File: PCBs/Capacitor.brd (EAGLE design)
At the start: 10 x 29.3 mm, 3 parts

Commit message: Updated
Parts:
- moved U$1 0.79 mm to (8.77, 19.9)
- moved C1 0.77 mm to (8.76, 12.1)
- moved U$2 0.76 mm to (8.76, 4.57)
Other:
- board size 10 x 29.3 mm -> 14.5 x 36.5 mm
- board text added: "care@pinwheel.in"
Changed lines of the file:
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@@
 <setting verticaltext="up"/>
 </settings>
-<grid distance="50" unitdist="mil" unit="mm" style="lines" multiple="1" display="yes" altdistance="5" altunitdist="mil" altunit="mm"/>
+<grid distance="0.5" unitdist="mm" unit="mm" style="lines" multiple="1" display="yes" altdistance="5" altunitdist="mil" altunit="mm"/>
 <layers>
 <layer number="1" name="Top" color="4" fill="1" visible="yes" active="yes"/>
@@
 <layer number="43" name="vRestrict" color="2" fill="10" visible="yes" active="yes"/>
 <layer number="44" name="Drills" color="7" fill="1" visible="no" active="yes"/>
-<layer number="45" name="Holes" color="7" fill="1" visible="no" active="yes"/>
+<layer number="45" name="Holes" color="7" fill="1" visible="yes" active="yes"/>
 <layer number="46" name="Milling" color="3" fill="1" visible="no" active="yes"/>
 <layer number="47" name="Measures" color="7" fill="1" visible="no" active="yes"/>
@@
 <board>
 <plain>
-<wire x1="3.048" y1="-2.54" x2="13.081" y2="-2.54" width="0" layer="20"/>
-<wire x1="13.081" y1="-2.54" x2="13.081" y2="26.73" width="0" layer="20"/>
-<wire x1="13.081" y1="26.73" x2="3.048" y2="26.73" width="0" layer="20"/>
-<wire x1="3.048" y1="26.73" x2="3.048" y2="-2.54" width="0" layer="20"/>
+<wire x1="14.292896875" y1="27" x2="3.207103125" y2="27" width="0" layer="20"/>
+<wire x1="3.207103125" y1="27" x2="1.5" y2="25.292896875" width="0" layer="20" curve="90"/>
+<wire x1="1.5" y1="25.292896875" x2="1.5" y2="-0.765165625" width="0" layer="20"/>
+<wire x1="1.5" y1="-0.765165625" x2="3.274834375" y2="-2.54" width="0" layer="20" curve="90"/>
+<wire x1="3.274834375" y1="-2.54" x2="14.225165625" y2="-2.54" width="0" layer="20"/>
+<wire x1="14.225165625" y1="-2.54" x2="16" y2="-0.765165625" width="0" layer="20" curve="90"/>
+<wire x1="16" y1="-0.765165625" x2="16" y2="25.292896875" width="0" layer="20"/>
+<wire x1="16" y1="25.292896875" x2="14.292896875" y2="27" width="0" layer="20" curve="90"/>
 <text x="12.192" y="9.144" size="0.8128" layer="21" rot="R90">Pinwheel Robotics </text>
 <text x="5.461" y="10.541" size="0.8128" layer="21" rot="R90">Capacitor</text>
+<hole x="3.43" y="24.981" drill="3"/>
+<hole x="14.003" y="24.903" drill="3"/>
+<hole x="3.548" y="-0.524" drill="3"/>
+<hole x="14.013" y="-0.54" drill="3"/>
+<wire x1="12" y1="-9" x2="11.5" y2="-9.5" width="0.1524" layer="20"/>
+<text x="15" y="21" size="1.778" layer="22" rot="MR270">care@pinwheel.in</text>
 </plain>
 <attributes>
@@
 </class>
 </classes>
-<designrules name="default">
+<designrules name="default *">
 <description language="de">&lt;b&gt;EAGLE Design Rules&lt;/b&gt;
 &lt;p&gt;
@@
 <param name="mdDrill" value="6mil"/>
 <param name="mdSmdStop" value="0mil"/>
-<param name="msWidth" value="6mil"/>
+<param name="msWidth" value="20mil"/>
 <param name="msDrill" value="0.35mm"/>
 <param name="msMicroVia" value="9.99mm"/>
@@
 <autorouter>
 <pass name="Default">
-<param name="RoutingGrid" value="50mil"/>
+<param name="RoutingGrid" value="0.25mm"/>
 <param name="AutoGrid" value="1"/>
 <param name="Efforts" value="0"/>
@@
 <param name="PrefDir.14" value="0"/>
 <param name="PrefDir.15" value="0"/>
-<param name="PrefDir.16" value="a"/>
+<param name="PrefDir.16" value="-"/>
 <param name="cfVia" value="8"/>
 <param name="cfNonPref" value="5"/>
@@
 </autorouter>
 <elements>
-<element name="C1" library="SparkFun-Capacitors" library_urn="urn:adsk.eagle:library:510" package="CAP-PTH-2.54" package3d_urn="urn:adsk.eagle:package:37435/1" value="22pF" x="8" y="12" smashed="yes" rot="R90">
-<attribute name="NAME" x="6.984" y="12" size="0.6096" layer="25" font="vector" ratio="20" rot="R90" align="bottom-center"/>
-<attribute name="PROD_ID" value="CAP-09128" x="25.78" y="27.24" size="1.778" layer="27" rot="R90" display="off"/>
-<attribute name="VALUE" x="9.016" y="12" size="0.6096" layer="27" font="vector" ratio="20" rot="R90" align="top-center"/>
+<element name="C1" library="SparkFun-Capacitors" library_urn="urn:adsk.eagle:library:510" package="CAP-PTH-2.54" package3d_urn="urn:adsk.eagle:package:37435/1" value="22pF" x="8.763" y="12.065" smashed="yes" rot="R90">
+<attribute name="NAME" x="7.747" y="12.065" size="0.6096" layer="25" font="vector" ratio="20" rot="R90" align="bottom-center"/>
+<attribute name="PROD_ID" value="CAP-09128" x="26.543" y="27.305" size="1.778" layer="27" rot="R90" display="off"/>
+<attribute name="VALUE" x="9.779" y="12.065" size="0.6096" layer="27" font="vector" ratio="20" rot="R90" align="top-center"/>
 </element>
-<element name="U$1" library="microbit" package="MICROBIT_PAD" value="MICROBIT_PAD" x="8" y="19.812" smashed="yes" rot="R180"/>
-<element name="U$2" library="microbit" package="MICROBIT_PAD" value="MICROBIT_PAD" x="8" y="4.572" smashed="yes"/>
+<element name="U$1" library="microbit" package="MICROBIT_PAD" value="MICROBIT_PAD" x="8.774" y="19.949" smashed="yes" rot="R180"/>
+<element name="U$2" library="microbit" package="MICROBIT_PAD" value="MICROBIT_PAD" x="8.762" y="4.572" smashed="yes"/>
 </elements>
 <signals>
@@
 <contactref element="C1" pad="1"/>
 <contactref element="U$2" pad="PAD"/>
-<wire x1="8.0772" y1="10.8204" x2="8" y2="10.73" width="0.1524" layer="16"/>
-<wire x1="8" y1="10.73" x2="8" y2="4.572" width="1.8" layer="16"/>
+<wire x1="8.75" y1="4.75" x2="8.75" y2="10.75" width="0.508" layer="16"/>
+<wire x1="8.75" y1="10.75" x2="8.763" y2="10.795" width="0.508" layer="16"/>
+<wire x1="8.75" y1="4.75" x2="8.762" y2="4.572" width="0.508" layer="16"/>
 </signal>
 <signal name="N$2">
 <contactref element="U$1" pad="PAD"/>
 <contactref element="C1" pad="2"/>
-<wire x1="8.0772" y1="13.5636" x2="8" y2="13.27" width="0.1524" layer="16"/>
-<wire x1="8.0772" y1="18.4404" x2="8.096790625" y2="18.459990625" width="0.1524" layer="16"/>
-<wire x1="8.096790625" y1="18.459990625" x2="8" y2="19.812" width="0" layer="19" extent="16-16"/>
-<wire x1="7.62" y1="19.05" x2="8.096790625" y2="18.459990625" width="0" layer="19" extent="16-16"/>
-<wire x1="8" y1="13.27" x2="8" y2="18.67" width="1.8" layer="16"/>
-<wire x1="8" y1="18.67" x2="7.62" y2="19.05" width="1.8" layer="16"/>
+<wire x1="8.75" y1="19.75" x2="8.75" y2="13.5" width="0.508" layer="16"/>
+<wire x1="8.75" y1="13.5" x2="8.763" y2="13.335" width="0.508" layer="16"/>
+<wire x1="8.75" y1="19.75" x2="8.774" y2="19.949" width="0.508" layer="16"/>
 </signal>
 </signals>

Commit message: New Update
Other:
- board size 14.5 x 36.5 mm -> 14.5 x 29.5 mm
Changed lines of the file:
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@@
 <drawing>
 <settings>
-<setting alwaysvectorfont="yes"/>
+<setting alwaysvectorfont="no"/>
 <setting verticaltext="up"/>
 </settings>
@@
 <text x="12.192" y="9.144" size="0.8128" layer="21" rot="R90">Pinwheel Robotics </text>
 <text x="5.461" y="10.541" size="0.8128" layer="21" rot="R90">Capacitor</text>
-<hole x="3.43" y="24.981" drill="3"/>
-<hole x="14.003" y="24.903" drill="3"/>
-<hole x="3.548" y="-0.524" drill="3"/>
-<hole x="14.013" y="-0.54" drill="3"/>
-<wire x1="12" y1="-9" x2="11.5" y2="-9.5" width="0.1524" layer="20"/>
+<hole x="3.5" y="25" drill="3"/>
+<hole x="14" y="25" drill="3"/>
+<hole x="3.5" y="-0.5" drill="3"/>
+<hole x="14" y="-0.5" drill="3"/>
 <text x="15" y="21" size="1.778" layer="22" rot="MR270">care@pinwheel.in</text>
 </plain>

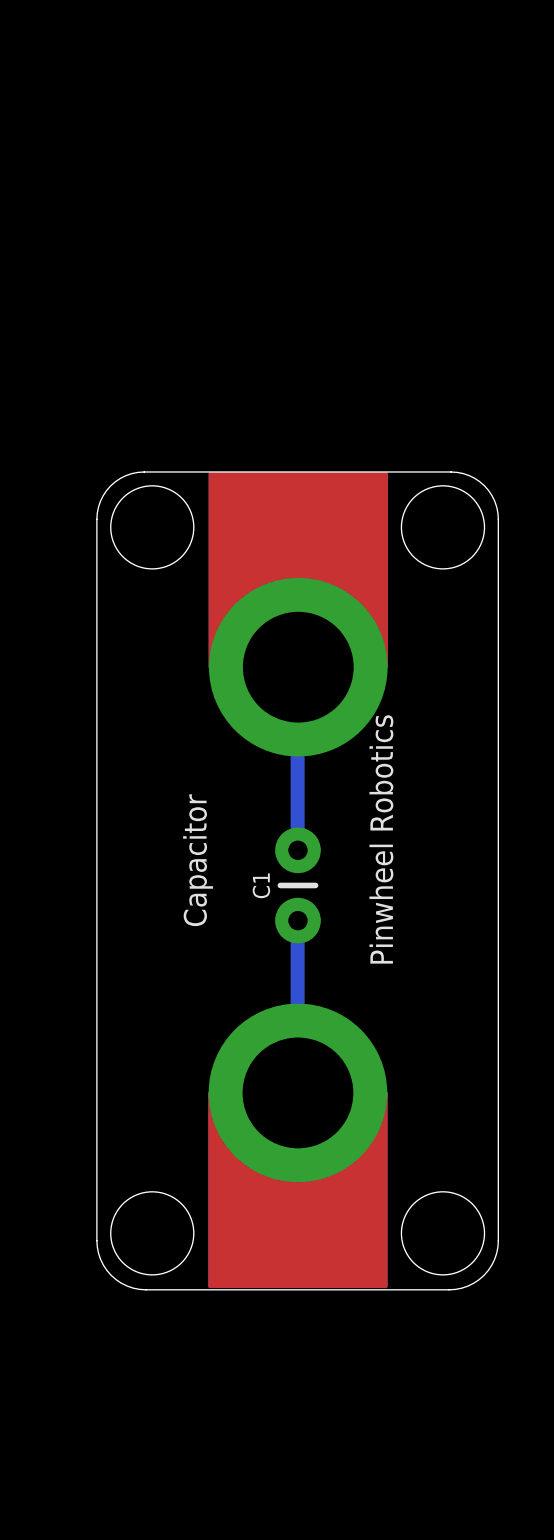
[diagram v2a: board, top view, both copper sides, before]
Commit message: New Update for board curv
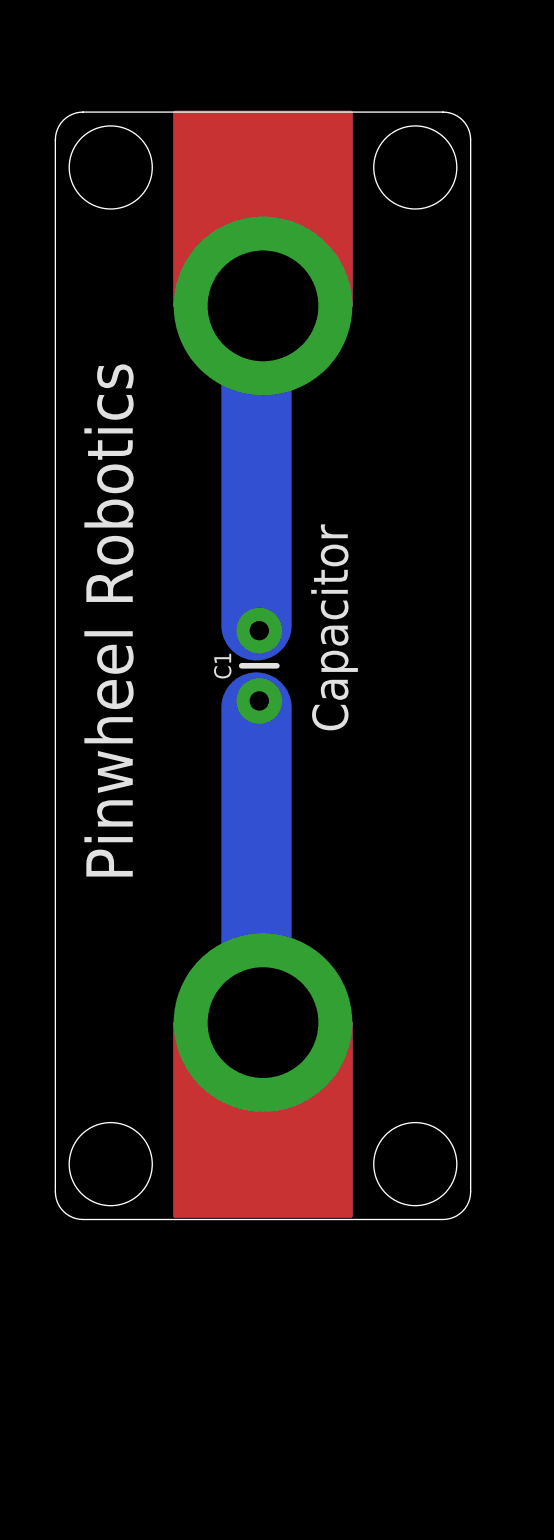
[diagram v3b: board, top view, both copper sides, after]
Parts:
- moved U$1 13.1 mm to (7.50, 33.0)
- moved C1 8.06 mm to (7.37, 20.0)
- moved U$2 2.84 mm to (7.50, 7.11)
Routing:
- net N$1: track 6.23 -> 11.8 mm
- net N$2: track 6.62 -> 11.8 mm
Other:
- board size 14.5 x 29.5 mm -> 15 x 40 mm
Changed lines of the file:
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@@
 <drawing>
 <settings>
-<setting alwaysvectorfont="no"/>
+<setting alwaysvectorfont="yes"/>
 <setting verticaltext="up"/>
 </settings>
@@
 <board>
 <plain>
-<wire x1="14.292896875" y1="27" x2="3.207103125" y2="27" width="0" layer="20"/>
-<wire x1="3.207103125" y1="27" x2="1.5" y2="25.292896875" width="0" layer="20" curve="90"/>
-<wire x1="1.5" y1="25.292896875" x2="1.5" y2="-0.765165625" width="0" layer="20"/>
-<wire x1="1.5" y1="-0.765165625" x2="3.274834375" y2="-2.54" width="0" layer="20" curve="90"/>
-<wire x1="3.274834375" y1="-2.54" x2="14.225165625" y2="-2.54" width="0" layer="20"/>
-<wire x1="14.225165625" y1="-2.54" x2="16" y2="-0.765165625" width="0" layer="20" curve="90"/>
-<wire x1="16" y1="-0.765165625" x2="16" y2="25.292896875" width="0" layer="20"/>
-<wire x1="16" y1="25.292896875" x2="14.292896875" y2="27" width="0" layer="20" curve="90"/>
-<text x="12.192" y="9.144" size="0.8128" layer="21" rot="R90">Pinwheel Robotics </text>
-<text x="5.461" y="10.541" size="0.8128" layer="21" rot="R90">Capacitor</text>
-<hole x="3.5" y="25" drill="3"/>
-<hole x="14" y="25" drill="3"/>
-<hole x="3.5" y="-0.5" drill="3"/>
-<hole x="14" y="-0.5" drill="3"/>
-<text x="15" y="21" size="1.778" layer="22" rot="MR270">care@pinwheel.in</text>
+<wire x1="1" y1="0" x2="14" y2="0" width="0" layer="20"/>
+<wire x1="14" y1="0" x2="15" y2="1" width="0" layer="20" curve="90"/>
+<wire x1="15" y1="1" x2="15" y2="39" width="0" layer="20"/>
+<wire x1="15" y1="39" x2="14" y2="40" width="0" layer="20" curve="90"/>
+<wire x1="14" y1="40" x2="1" y2="40" width="0" layer="20"/>
+<wire x1="1" y1="40" x2="0" y2="39" width="0" layer="20" curve="90"/>
+<wire x1="0" y1="39" x2="0" y2="1" width="0" layer="20"/>
+<wire x1="0" y1="1" x2="1" y2="0" width="0" layer="20" curve="90"/>
+<text x="2.795" y="12.184" size="1.6764" layer="21" rot="R90">Pinwheel Robotics </text>
+<text x="10.564" y="17.581" size="1.27" layer="21" rot="R90">Capacitor</text>
+<hole x="2" y="38" drill="3"/>
+<hole x="13" y="38" drill="3"/>
+<hole x="2" y="2" drill="3"/>
+<hole x="13" y="2" drill="3"/>
+<text x="14.603" y="30.04" size="1.778" layer="22" rot="MR270">care@pinwheel.in</text>
 </plain>
 <attributes>
@@
 </autorouter>
 <elements>
-<element name="C1" library="SparkFun-Capacitors" library_urn="urn:adsk.eagle:library:510" package="CAP-PTH-2.54" package3d_urn="urn:adsk.eagle:package:37435/1" value="22pF" x="8.763" y="12.065" smashed="yes" rot="R90">
-<attribute name="NAME" x="7.747" y="12.065" size="0.6096" layer="25" font="vector" ratio="20" rot="R90" align="bottom-center"/>
-<attribute name="PROD_ID" value="CAP-09128" x="26.543" y="27.305" size="1.778" layer="27" rot="R90" display="off"/>
-<attribute name="VALUE" x="9.779" y="12.065" size="0.6096" layer="27" font="vector" ratio="20" rot="R90" align="top-center"/>
+<element name="C1" library="SparkFun-Capacitors" library_urn="urn:adsk.eagle:library:510" package="CAP-PTH-2.54" package3d_urn="urn:adsk.eagle:package:37435/1" value="22pF" x="7.366" y="20" smashed="yes" rot="R90">
+<attribute name="NAME" x="6.35" y="20" size="0.6096" layer="25" font="vector" ratio="20" rot="R90" align="bottom-center"/>
+<attribute name="PROD_ID" value="CAP-09128" x="25.146" y="35.24" size="1.778" layer="27" rot="R90" display="off"/>
+<attribute name="VALUE" x="8.382" y="20" size="0.6096" layer="27" font="vector" ratio="20" rot="R90" align="top-center"/>
 </element>
-<element name="U$1" library="microbit" package="MICROBIT_PAD" value="MICROBIT_PAD" x="8.774" y="19.949" smashed="yes" rot="R180"/>
-<element name="U$2" library="microbit" package="MICROBIT_PAD" value="MICROBIT_PAD" x="8.762" y="4.572" smashed="yes"/>
+<element name="U$1" library="microbit" package="MICROBIT_PAD" value="MICROBIT_PAD" x="7.5" y="33" smashed="yes" rot="R180"/>
+<element name="U$2" library="microbit" package="MICROBIT_PAD" value="MICROBIT_PAD" x="7.5" y="7.112" smashed="yes"/>
 </elements>
 <signals>
@@
 <contactref element="C1" pad="1"/>
 <contactref element="U$2" pad="PAD"/>
-<wire x1="8.75" y1="4.75" x2="8.75" y2="10.75" width="0.508" layer="16"/>
-<wire x1="8.75" y1="10.75" x2="8.763" y2="10.795" width="0.508" layer="16"/>
-<wire x1="8.75" y1="4.75" x2="8.762" y2="4.572" width="0.508" layer="16"/>
+<wire x1="7.2644" y1="7.2644" x2="7.2644" y2="18.4912" width="2.54" layer="16"/>
+<wire x1="7.2644" y1="18.4912" x2="7.366" y2="18.73" width="0.508" layer="16"/>
+<wire x1="7.2644" y1="7.2644" x2="7.5" y2="7.112" width="0.508" layer="16"/>
 </signal>
 <signal name="N$2">
 <contactref element="U$1" pad="PAD"/>
 <contactref element="C1" pad="2"/>
-<wire x1="8.75" y1="19.75" x2="8.75" y2="13.5" width="0.508" layer="16"/>
-<wire x1="8.75" y1="13.5" x2="8.763" y2="13.335" width="0.508" layer="16"/>
-<wire x1="8.75" y1="19.75" x2="8.774" y2="19.949" width="0.508" layer="16"/>
+<wire x1="7.2644" y1="32.6898" x2="7.2644" y2="21.463" width="2.54" layer="16"/>
+<wire x1="7.2644" y1="21.463" x2="7.366" y2="21.27" width="0.508" layer="16"/>
+<wire x1="7.2644" y1="32.6898" x2="7.5" y2="33" width="0.508" layer="16"/>
 </signal>
 </signals>

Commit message: Dimension added
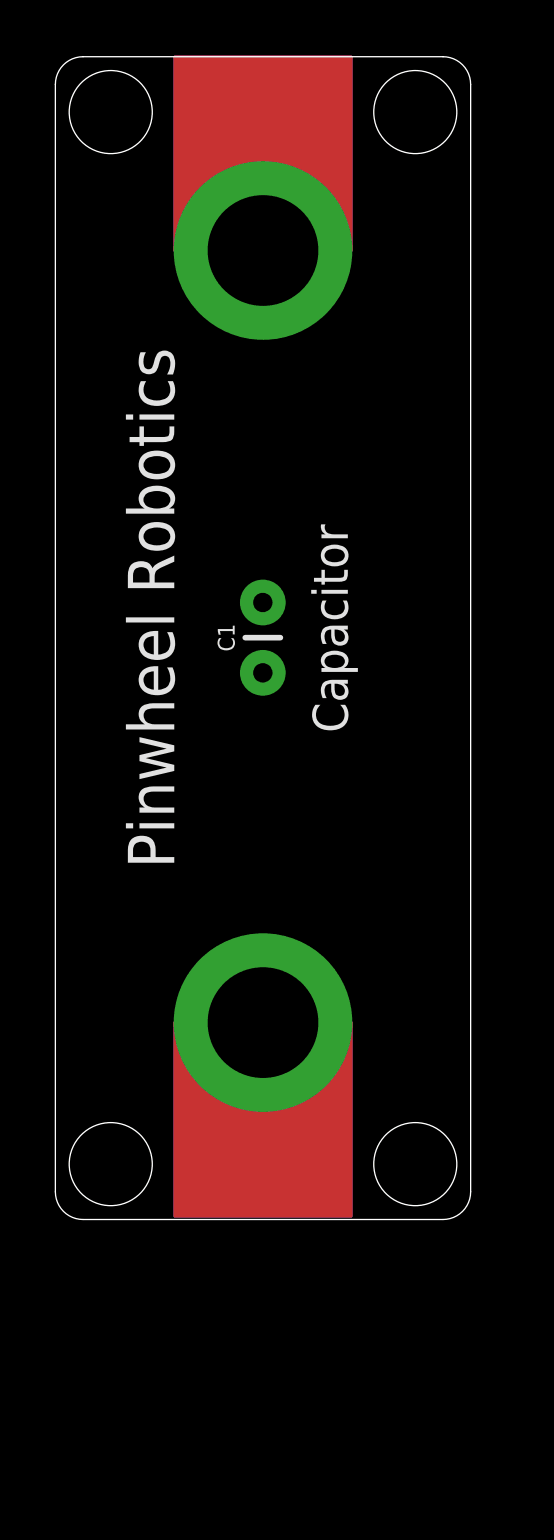
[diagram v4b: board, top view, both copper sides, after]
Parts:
- moved U$1 2.00 mm to (7.50, 35.0)
- moved C1 1.02 mm to (7.49, 21.0)
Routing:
- net N$2: track 11.8 -> 0.00 mm
- net N$1: track 11.8 -> 0.00 mm
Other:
- board size 15 x 40 mm -> 15 x 42 mm
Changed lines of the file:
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@@
 <drawing>
 <settings>
-<setting alwaysvectorfont="yes"/>
+<setting alwaysvectorfont="no"/>
 <setting verticaltext="up"/>
 </settings>
@@
 <board>
 <plain>
+<wire x1="0" y1="41" x2="0" y2="1" width="0" layer="20"/>
+<wire x1="0" y1="1" x2="1" y2="0" width="0" layer="20" curve="90"/>
 <wire x1="1" y1="0" x2="14" y2="0" width="0" layer="20"/>
 <wire x1="14" y1="0" x2="15" y2="1" width="0" layer="20" curve="90"/>
-<wire x1="15" y1="1" x2="15" y2="39" width="0" layer="20"/>
-<wire x1="15" y1="39" x2="14" y2="40" width="0" layer="20" curve="90"/>
-<wire x1="14" y1="40" x2="1" y2="40" width="0" layer="20"/>
-<wire x1="1" y1="40" x2="0" y2="39" width="0" layer="20" curve="90"/>
-<wire x1="0" y1="39" x2="0" y2="1" width="0" layer="20"/>
-<wire x1="0" y1="1" x2="1" y2="0" width="0" layer="20" curve="90"/>
-<text x="2.795" y="12.184" size="1.6764" layer="21" rot="R90">Pinwheel Robotics </text>
+<wire x1="15" y1="1" x2="15" y2="41" width="0" layer="20"/>
+<wire x1="15" y1="41" x2="14" y2="42" width="0" layer="20" curve="90"/>
+<wire x1="14" y1="42" x2="1" y2="42" width="0" layer="20"/>
+<wire x1="1" y1="42" x2="0" y2="41" width="0" layer="20" curve="90"/>
+<text x="4.295" y="12.684" size="1.6764" layer="21" rot="R90">Pinwheel Robotics </text>
 <text x="10.564" y="17.581" size="1.27" layer="21" rot="R90">Capacitor</text>
-<hole x="2" y="38" drill="3"/>
-<hole x="13" y="38" drill="3"/>
+<hole x="2" y="40" drill="3"/>
+<hole x="13" y="40" drill="3"/>
 <hole x="2" y="2" drill="3"/>
 <hole x="13" y="2" drill="3"/>
-<text x="14.603" y="30.04" size="1.778" layer="22" rot="MR270">care@pinwheel.in</text>
+<text x="13.103" y="31.54" size="1.778" layer="22" rot="MR270">care@pinwheel.in</text>
 </plain>
 <attributes>
@@
 </autorouter>
 <elements>
-<element name="C1" library="SparkFun-Capacitors" library_urn="urn:adsk.eagle:library:510" package="CAP-PTH-2.54" package3d_urn="urn:adsk.eagle:package:37435/1" value="22pF" x="7.366" y="20" smashed="yes" rot="R90">
-<attribute name="NAME" x="6.35" y="20" size="0.6096" layer="25" font="vector" ratio="20" rot="R90" align="bottom-center"/>
-<attribute name="PROD_ID" value="CAP-09128" x="25.146" y="35.24" size="1.778" layer="27" rot="R90" display="off"/>
-<attribute name="VALUE" x="8.382" y="20" size="0.6096" layer="27" font="vector" ratio="20" rot="R90" align="top-center"/>
+<element name="C1" library="SparkFun-Capacitors" library_urn="urn:adsk.eagle:library:510" package="CAP-PTH-2.54" package3d_urn="urn:adsk.eagle:package:37435/1" value="22pF" x="7.493" y="21.016" smashed="yes" rot="R90">
+<attribute name="NAME" x="6.477" y="21.016" size="0.6096" layer="25" font="vector" ratio="20" rot="R90" align="bottom-center"/>
+<attribute name="PROD_ID" value="CAP-09128" x="25.273" y="36.256" size="1.778" layer="27" rot="R90" display="off"/>
+<attribute name="VALUE" x="8.509" y="21.016" size="0.6096" layer="27" font="vector" ratio="20" rot="R90" align="top-center"/>
 </element>
-<element name="U$1" library="microbit" package="MICROBIT_PAD" value="MICROBIT_PAD" x="7.5" y="33" smashed="yes" rot="R180"/>
+<element name="U$1" library="microbit" package="MICROBIT_PAD" value="MICROBIT_PAD" x="7.5" y="35" smashed="yes" rot="R180"/>
 <element name="U$2" library="microbit" package="MICROBIT_PAD" value="MICROBIT_PAD" x="7.5" y="7.112" smashed="yes"/>
 </elements>
@@
 <contactref element="C1" pad="1"/>
 <contactref element="U$2" pad="PAD"/>
-<wire x1="7.2644" y1="7.2644" x2="7.2644" y2="18.4912" width="2.54" layer="16"/>
-<wire x1="7.2644" y1="18.4912" x2="7.366" y2="18.73" width="0.508" layer="16"/>
-<wire x1="7.2644" y1="7.2644" x2="7.5" y2="7.112" width="0.508" layer="16"/>
+<wire x1="7.5" y1="7.112" x2="7.493" y2="19.746" width="0" layer="19" extent="1-1"/>
 </signal>
 <signal name="N$2">
 <contactref element="U$1" pad="PAD"/>
 <contactref element="C1" pad="2"/>
-<wire x1="7.2644" y1="32.6898" x2="7.2644" y2="21.463" width="2.54" layer="16"/>
-<wire x1="7.2644" y1="21.463" x2="7.366" y2="21.27" width="0.508" layer="16"/>
-<wire x1="7.2644" y1="32.6898" x2="7.5" y2="33" width="0.508" layer="16"/>
+<wire x1="7.493" y1="22.286" x2="7.5" y2="35" width="0" layer="19" extent="1-1"/>
 </signal>
 </signals>
